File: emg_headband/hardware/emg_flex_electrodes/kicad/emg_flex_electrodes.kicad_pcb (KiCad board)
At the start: 2 copper layers, 298 x 43 mm, 8 parts, among them J1 TO MAIN BOARD J6

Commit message: Flex: follow main board J6 pinout and right-edge entry
J6 now carries CH1 on 2-4, CH2 on 6-8, CH3 on 10-12 and takes the FPC
from the board's right edge, so the tail runs along the subject's right.
TAIL_SIDE mirrors the layout; DRC still clean.

Co-Authored-By: Claude Opus 5.5 (1M context) <noreply@anthropic.com>
Claude-Session: https://claude.ai/code/session_014gX5rSabikoFKBd7bBuHGf
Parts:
- E1: value CH1+ FRONTALIS L -> CH1+ FRONTALIS R
- E2: value CH1- FRONTALIS L -> CH1- FRONTALIS R
- E3: value CH2+ CORRUGATOR R -> CH2+ CORRUGATOR L
- E4: value CH2- CORRUGATOR R -> CH2- CORRUGATOR L
- E5: value CH3+ TEMPORALIS L -> CH3+ TEMPORALIS R
- E6: value CH3- TEMPORALIS L -> CH3- TEMPORALIS R
- moved E4 330.0 mm to (365.0, 112.0)
- moved E3 300.0 mm to (350.0, 112.0)
- moved E7 280.0 mm to (340.0, 83.0)
- moved J1 247.1 mm to (76.5, 86.0)
- moved E1 220.0 mm to (310.0, 86.0)
- moved E2 220.0 mm to (310.0, 106.0)
- moved E5 110.0 mm to (255.0, 86.0)
- moved E6 110.0 mm to (255.0, 106.0)
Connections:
- J1 pad 10: CH1N -> CH3P
- J1 pad 11: CH1P -> CH3N
- J1 pad 2: CH3N -> CH1P
- J1 pad 3: CH3P -> CH1N
- J1 pad 6: CH2N -> CH2P
- J1 pad 7: CH2P -> CH2N
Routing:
- net CH3N: track 203.6 -> 194.6 mm
- net CH1P: track 250.4 -> 259.4 mm
- net CH1N: track 250.4 -> 257.4 mm
- net CH3P: track 201.6 -> 194.6 mm
- net CH2P: track 299.1 -> 300.1 mm
- net CH2N: track 315.1 -> 314.1 mm
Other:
- outline, holes or cut-outs redrawn
- board text added: "CORRUGATOR L (CH2)"
- board text added: "FRONTALIS R (CH1)"
- board text added: "TEMPORALIS R (CH3)"
- board text removed: "CORRUGATOR R (CH2)"
- board text removed: "FRONTALIS L (CH1)"
- board text removed: "TEMPORALIS L (CH3)"

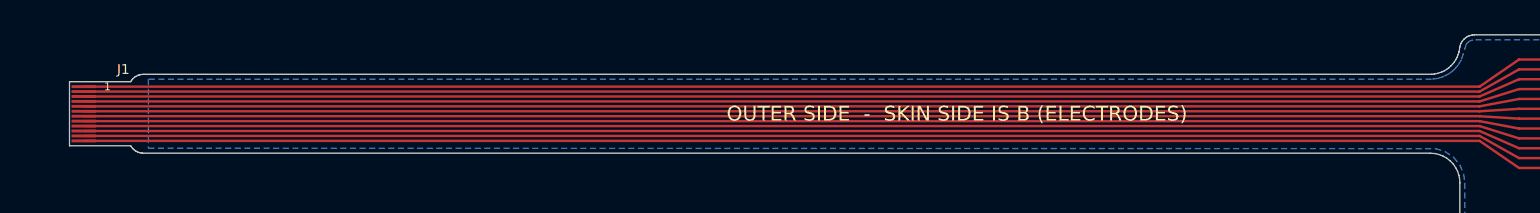
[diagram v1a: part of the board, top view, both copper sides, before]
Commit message: Flex: size tail for a 58 cm head
Pin order rechecked against main board J6 pads (57179a6): unchanged.

Co-Authored-By: Claude Opus 5.5 (1M context) <noreply@anthropic.com>
Claude-Session: https://claude.ai/code/session_014gX5rSabikoFKBd7bBuHGf
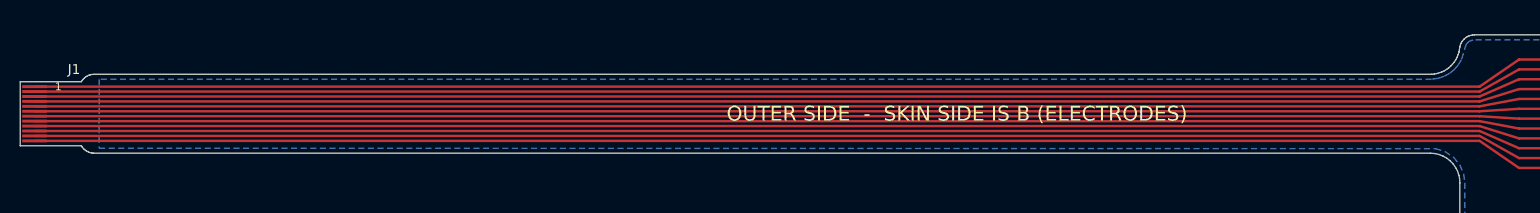
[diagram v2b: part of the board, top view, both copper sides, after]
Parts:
- moved J1 5.00 mm to (71.5, 86.0)
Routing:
- net REF: track 621.3 -> 636.3 mm
- net AGND: track 445.3 -> 460.3 mm
- net CH3P: track 194.6 -> 199.6 mm
- net CH3N: track 194.6 -> 199.6 mm
- net CH2P: track 300.1 -> 305.1 mm
- net CH2N: track 314.1 -> 319.1 mm
- net CH1P: track 259.4 -> 264.4 mm
- net CH1N: track 257.4 -> 262.4 mm
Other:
- board size 298 x 43 mm -> 303 x 43 mm

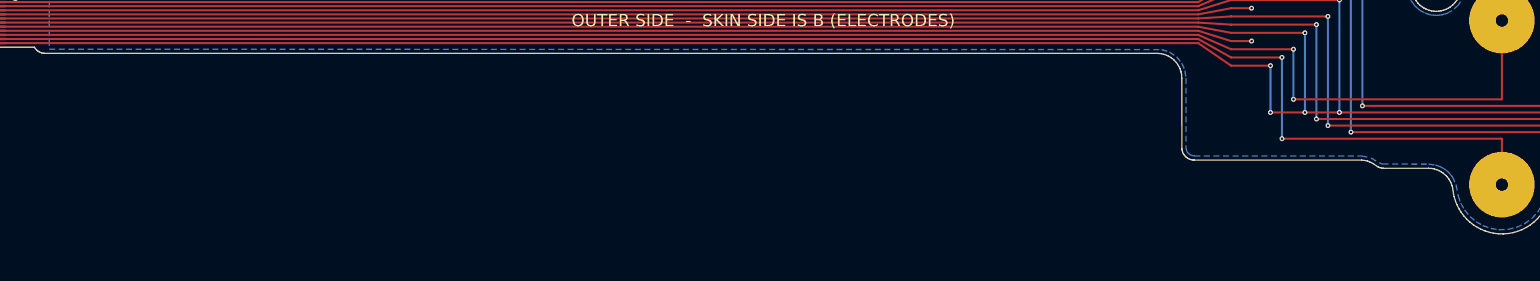
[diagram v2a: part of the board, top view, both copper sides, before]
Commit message: Flex: add schematic, project libraries and ear keep-out
The generator now writes a full KiCad project: schematic linked to the
board by symbol UUIDs, emg_flex symbol and footprint libraries with lib
tables, and the routed board. The crossover block steps up before the
ear and the generator asserts 12 mm clearance to a modelled pinna
(21 mm now). DRC clean; schematic netlist matches every board pad.

Co-Authored-By: Claude Opus 5.5 (1M context) <noreply@anthropic.com>
Claude-Session: https://claude.ai/code/session_014gX5rSabikoFKBd7bBuHGf
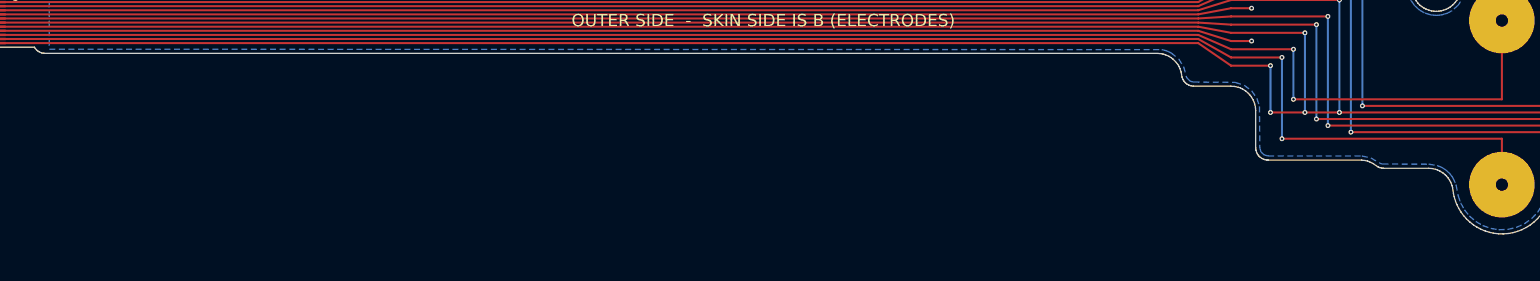
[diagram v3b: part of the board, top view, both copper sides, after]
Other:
- outline, holes or cut-outs redrawn
- board text added: "EAR R (keep-out 12 mm)"
